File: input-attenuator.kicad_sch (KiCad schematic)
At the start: 92 parts, among them J1 DC_INTF, J2 RF_IN, J3 RX_1_RF, J4 RX_2_RF, K1 EE2-5TNU-L, K2 EE2-5TNU-L, K3 EE2-5TNU-L, K4 EE2-5TNU-L, Q1 BC858, Q2 BC858, Q3 MMBT3904, Q4 BC858, Q5 BC858, Q6 BC858, Q7 BC858, Q8 BC858, Q9 BC858, U1 74HC00, U2 74HC00, U3 74HC00, U4 74HC00, U5 74HC00, U6 74HC595

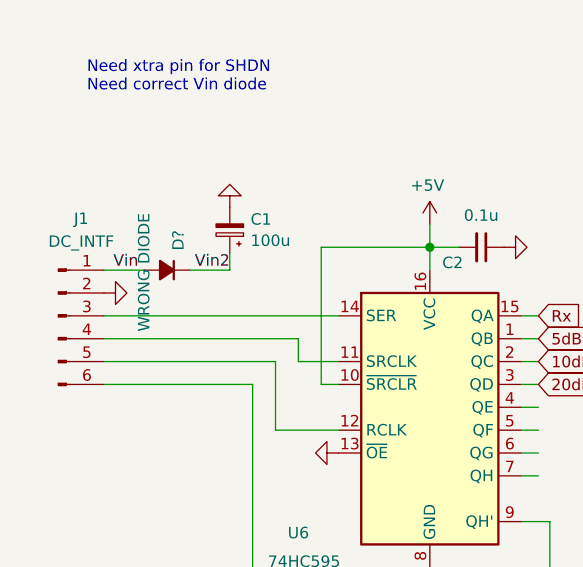
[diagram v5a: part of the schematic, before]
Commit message: Updated input pin header and Vin diode
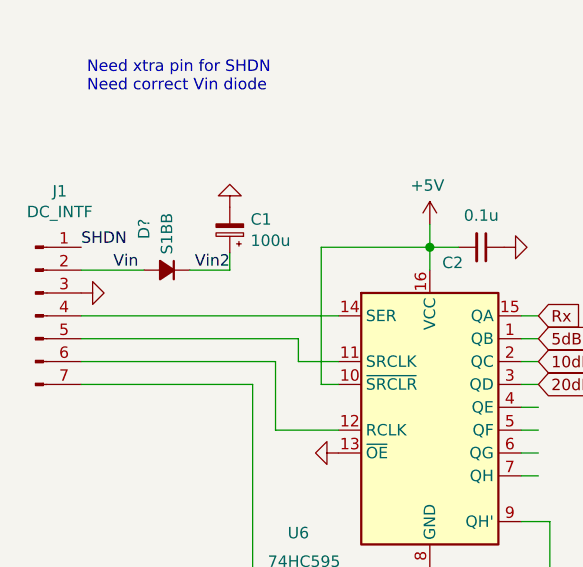
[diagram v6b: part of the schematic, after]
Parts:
- removed J1: DC_INTF, Connector_PinHeader_2.54mm:PinHeader_1x06_P2.54mm_Vertical, symbol Connector:Conn_01x06_Male
- added J1: DC_INTF, Connector_PinHeader_2.54mm:PinHeader_1x07_P2.54mm_Vertical, symbol Connector:Conn_01x07_Male
- D?: value WRONG DIODE -> S1BB; footprint Diode_SMD:D_SOD-323 -> Diode_SMD:D_SMB_Handsoldering
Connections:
- net GND: now also J1.3 (Pin_3)
- net SHDN: now also J1.1 (Pin_1)
- net Vin: now also J1.2 (Pin_2)
- net at U6.11 (SRCLK): now also J1.5 (Pin_5)
- net at U6.12 (RCLK): now also J1.6 (Pin_6)
- net at U6.14 (SER): now also J1.4 (Pin_4)
- net at U6.9 (QH'): now also J1.7 (Pin_7)
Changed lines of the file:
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@@
   (junction (at 259.715 40.005) (diameter 1.016) (color 0 0 0 0))
   (junction (at 259.715 57.15) (diameter 1.016) (color 0 0 0 0))
-  (wire (pts (xy 22.86 152.4) (xy 27.305 152.4))
+  (wire (pts (xy 20.32 152.4) (xy 27.305 152.4))
     (stroke (width 0) (type solid) (color 0 0 0 0))
   )
-  (wire (pts (xy 22.86 157.48) (xy 48.895 157.48))
+  (wire (pts (xy 20.32 157.48) (xy 48.895 157.48))
     (stroke (width 0) (type solid) (color 0 0 0 0))
   )
-  (wire (pts (xy 22.86 160.02) (xy 44.45 160.02))
+  (wire (pts (xy 20.32 160.02) (xy 44.45 160.02))
     (stroke (width 0) (type solid) (color 0 0 0 0))
   )
-  (wire (pts (xy 22.86 162.56) (xy 41.91 162.56))
+  (wire (pts (xy 20.32 162.56) (xy 41.91 162.56))
     (stroke (width 0) (type solid) (color 0 0 0 0))
   )
-  (wire (pts (xy 22.86 165.1) (xy 39.37 165.1))
+  (wire (pts (xy 20.32 165.1) (xy 39.37 165.1))
     (stroke (width 0) (type solid) (color 0 0 0 0))
   )
@@
     (effects (font (size 1.27 1.27)) (justify left bottom))
   )
+  (label "SHDN" (at 20.32 149.86 0)
+    (effects (font (size 1.27 1.27)) (justify left bottom))
+  )
   (label "PowerDn" (at 26.67 87.63 180)
     (effects (font (size 1.27 1.27)) (justify right bottom))
@@
     (pin "1")
   )
-  (symbol (lib_id "power:GND") (at 22.86 154.94 90) (unit 1)
+  (symbol (lib_id "power:GND") (at 20.32 154.94 90) (unit 1)
     (in_bom yes) (on_board yes)
-    (property "Reference" "#PWR0115" (id 0) (at 29.21 154.94 0)
+    (property "Reference" "#PWR0115" (id 0) (at 26.67 154.94 0)
       (effects (font (size 1.27 1.27)) hide)
     )
-    (property "Value" "GND" (id 1) (at 27.3558 154.813 0)
+    (property "Value" "GND" (id 1) (at 24.8158 154.813 0)
       (effects (font (size 1.27 1.27)) hide)
     )
-    (property "Footprint" "" (id 2) (at 22.86 154.94 0)
+    (property "Footprint" "" (id 2) (at 20.32 154.94 0)
       (effects (font (size 1.27 1.27)) hide)
     )
-    (property "Datasheet" "" (id 3) (at 22.86 154.94 0)
+    (property "Datasheet" "" (id 3) (at 20.32 154.94 0)
       (effects (font (size 1.27 1.27)) hide)
     )
@@
     (pin "2")
   )
+  (symbol (lib_id "Comparator:LM339") (at 149.225 172.085 0) (unit 5)
+    (in_bom yes) (on_board yes)
+    (property "Reference" "U?" (id 0) (at 149.225 162.7948 0))
+    (property "Value" "LP339" (id 1) (at 149.225 165.093 0))
+    (property "Footprint" "" (id 2) (at 147.955 169.545 0)
+      (effects (font (size 1.27 1.27)) hide)
+    )
+    (property "Datasheet" "https://www.st.com/resource/en/datasheet/lm139.pdf" (id 3) (at 150.495 167.005 0)
+      (effects (font (size 1.27 1.27)) hide)
+    )
+    (pin "12")
+    (pin "3")
+  )
   (symbol (lib_id "Device:D_Small_ALT") (at 29.21 49.53 270) (mirror x) (unit 1)
     (in_bom yes) (on_board yes)
@@
   (symbol (lib_id "Device:D_Small_ALT") (at 29.845 152.4 180) (unit 1)
     (in_bom yes) (on_board yes)
-    (property "Reference" "D?" (id 0) (at 31.115 147.955 90)
+    (property "Reference" "D?" (id 0) (at 27.305 146.685 90)
       (effects (font (size 1.27 1.27)) (justify left))
     )
-    (property "Value" "WRONG DIODE" (id 1) (at 27.305 146.05 90)
+    (property "Value" "S1BB" (id 1) (at 29.845 146.05 90)
       (effects (font (size 1.27 1.27)) (justify left))
     )
-    (property "Footprint" "Diode_SMD:D_SOD-323" (id 2) (at 29.845 152.4 90)
+    (property "Footprint" "Diode_SMD:D_SMB_Handsoldering" (id 2) (at 29.845 152.4 90)
       (effects (font (size 1.27 1.27)) hide)
     )
@@
     (pin "7")
   )
-  (symbol (lib_id "Comparator:LM339") (at 149.225 172.085 0) (unit 5)
-    (in_bom yes) (on_board yes)
-    (property "Reference" "U?" (id 0) (at 149.225 162.7948 0))
-    (property "Value" "LP339" (id 1) (at 149.225 165.093 0))
-    (property "Footprint" "" (id 2) (at 147.955 169.545 0)
-      (effects (font (size 1.27 1.27)) hide)
-    )
-    (property "Datasheet" "https://www.st.com/resource/en/datasheet/lm139.pdf" (id 3) (at 150.495 167.005 0)
-      (effects (font (size 1.27 1.27)) hide)
-    )
-    (pin "12")
-    (pin "3")
-  )
   (symbol (lib_id "Connector:Conn_Coaxial") (at 19.685 32.385 0) (mirror y) (unit 1)
     (in_bom yes) (on_board yes)
@@
     (pin "2")
   )
-  (symbol (lib_id "Connector:Conn_01x06_Male") (at 17.78 157.48 0) (unit 1)
+  (symbol (lib_id "Connector:Conn_01x07_Male") (at 15.24 157.48 0) (unit 1)
     (in_bom yes) (on_board yes)
-    (property "Reference" "J1" (id 0) (at 20.32 146.685 0))
-    (property "Value" "DC_INTF" (id 1) (at 20.32 149.225 0))
-    (property "Footprint" "Connector_PinHeader_2.54mm:PinHeader_1x06_P2.54mm_Vertical" (id 2) (at 17.78 157.48 0)
+    (property "Reference" "J1" (id 0) (at 17.9324 143.6328 0))
+    (property "Value" "DC_INTF" (id 1) (at 17.9324 145.9315 0))
+    (property "Footprint" "Connector_PinHeader_2.54mm:PinHeader_1x07_P2.54mm_Vertical" (id 2) (at 15.24 157.48 0)
       (effects (font (size 1.27 1.27)) hide)
     )
-    (property "Datasheet" "~" (id 3) (at 17.78 157.48 0)
+    (property "Datasheet" "~" (id 3) (at 15.24 157.48 0)
       (effects (font (size 1.27 1.27)) hide)
     )
@@
     (pin "5")
     (pin "6")
+    (pin "7")
   )
   (symbol (lib_id "Transistor_BJT:BC858") (at 40.64 66.04 0) (mirror y) (unit 1)
@@
     )
     (path "/9801f823-24c1-4f5d-bf6c-e2a3a0a8f252"
-      (reference "D?") (unit 1) (value "WRONG DIODE") (footprint "Diode_SMD:D_SOD-323")
+      (reference "D?") (unit 1) (value "S1BB") (footprint "Diode_SMD:D_SMB_Handsoldering")
     )
-    (path "/00000000-0000-0000-0000-00005f2d8ca1"
-      (reference "J1") (unit 1) (value "DC_INTF") (footprint "Connector_PinHeader_2.54mm:PinHeader_1x06_P2.54mm_Vertical")
+    (path "/92e7aac3-ac59-4653-8577-27b028dac29e"
+      (reference "J1") (unit 1) (value "DC_INTF") (footprint "Connector_PinHeader_2.54mm:PinHeader_1x07_P2.54mm_Vertical")
     )
     (path "/5687a9c9-05f1-4ecb-9b08-f88b6a240510"

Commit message: lookAtC
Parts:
- removed K? (x3): EE2-5TNU-L, Relay_SMD:Relay_DPDT_Kemet_EE2_NU_DoubleCoil, symbol rf-designers:EE2-5TNU-L
- removed R?: 180k, Resistor_SMD:R_0805_2012Metric, symbol Device:R_Small_US
- removed R? (x2): 1M, Resistor_SMD:R_0805_2012Metric, symbol Device:R_Small_US
- added J2: DC_INTF, Connector_PinHeader_2.54mm:PinHeader_1x07_P2.54mm_Vertical, symbol Connector:Conn_01x07_Male
- C1: value 100u -> 10000u
- U8: renamed from U?; footprint (none) -> Package_SO:SO-14_3.9x8.65mm_P1.27mm
- gave numbers to parts that had none: 16
- renumbered J2 to J5
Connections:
- net +5V: now also U8.6 (-); no longer U8.4 (-)
- net GND: now also J1.2 (Pin_2), J2.2 (Pin_2); no longer J1.3 (Pin_3)
- net PowerDn: now also U8.1; no longer U8.2
- net SHDN: now also J1.7 (Pin_7), J2.7 (Pin_7); no longer J1.1 (Pin_1)
- net Vin: now also J1.1 (Pin_1), J2.1 (Pin_1); no longer J1.2 (Pin_2)
- net at U6.11 (SRCLK): now also J1.4 (Pin_4), J2.4 (Pin_4); no longer J1.5 (Pin_5)
- net at U6.12 (RCLK): now also J1.5 (Pin_5); no longer J1.6 (Pin_6)
- net at U6.14 (SER): now also J1.3 (Pin_3), J2.3 (Pin_3); no longer J1.4 (Pin_4)
- net at U6.9 (QH'): now also J1.6 (Pin_6), J2.5 (Pin_5); no longer J1.7 (Pin_7)
- net at R31.1, R33.1, U8.2: now also U8.7 (+); no longer U8.5 (+)
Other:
- note added: "To next shift register"
- note removed: "Need xtra pin for SHDN Need correct Vin diode"
- moved on the sheet: J1

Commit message: final
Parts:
- removed unit 2 of U8
- added C8: 2200u, Capacitor_THT:CP_Radial_D12.5mm_P7.50mm, symbol Device:CP_Small
- C1: value 10000u -> 2200u; footprint Capacitor_SMD:CP_Elec_6.3x5.4_Nichicon -> Capacitor_THT:CP_Radial_D12.5mm_P7.50mm
- U6: footprint Package_SO:SO-16_5.3x10.2mm_P1.27mm -> Package_SO:SO-16_3.9x9.9mm_P1.27mm
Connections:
- net 20dB: now also U6.1 (QB); no longer U6.3 (QD)
- net 5dB: now also U6.3 (QD); no longer U6.1 (QB)
- net GND: now also C8.2
- net PowerDn: now also R31.1, R33.1, U8.2
- net Vin2: now also C8.1
- net at J1.4 (Pin_4), J2.4 (Pin_4): now also U6.12 (RCLK); no longer U6.11 (SRCLK)
- net at J1.5 (Pin_5): now also U6.11 (SRCLK); no longer U6.12 (RCLK)
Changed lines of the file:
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@@
   (junction (at 29.845 160.02) (diameter 1.016) (color 0 0 0 0))
   (junction (at 32.385 165.1) (diameter 1.016) (color 0 0 0 0))
+  (junction (at 36.83 152.4) (diameter 1.016) (color 0 0 0 0))
   (junction (at 38.1 40.005) (diameter 1.016) (color 0 0 0 0))
   (junction (at 38.1 57.15) (diameter 1.016) (color 0 0 0 0))
@@
     (stroke (width 0) (type solid) (color 0 0 0 0))
   )
-  (wire (pts (xy 20.32 162.56) (xy 41.91 162.56))
+  (wire (pts (xy 20.32 162.56) (xy 48.895 162.56))
     (stroke (width 0) (type solid) (color 0 0 0 0))
   )
@@
     (stroke (width 0) (type solid) (color 0 0 0 0))
   )
+  (wire (pts (xy 36.83 152.4) (xy 40.64 152.4))
+    (stroke (width 0) (type solid) (color 0 0 0 0))
+  )
   (wire (pts (xy 38.1 38.1) (xy 38.1 40.005))
     (stroke (width 0) (type solid) (color 0 0 0 0))
@@
     (stroke (width 0) (type solid) (color 0 0 0 0))
   )
-  (wire (pts (xy 41.91 85.09) (xy 46.99 85.09))
-    (stroke (width 0) (type solid) (color 0 0 0 0))
-  )
-  (wire (pts (xy 41.91 90.805) (xy 41.91 85.09))
+  (wire (pts (xy 40.64 152.4) (xy 40.64 150.495))
     (stroke (width 0) (type solid) (color 0 0 0 0))
   )
-  (wire (pts (xy 41.91 162.56) (xy 41.91 170.18))
+  (wire (pts (xy 41.91 85.09) (xy 46.99 85.09))
     (stroke (width 0) (type solid) (color 0 0 0 0))
   )
-  (wire (pts (xy 41.91 170.18) (xy 48.895 170.18))
+  (wire (pts (xy 41.91 90.805) (xy 41.91 85.09))
     (stroke (width 0) (type solid) (color 0 0 0 0))
   )
-  (wire (pts (xy 44.45 160.02) (xy 44.45 162.56))
+  (wire (pts (xy 44.45 160.02) (xy 44.45 170.18))
     (stroke (width 0) (type solid) (color 0 0 0 0))
   )
-  (wire (pts (xy 44.45 162.56) (xy 48.895 162.56))
+  (wire (pts (xy 44.45 170.18) (xy 48.895 170.18))
     (stroke (width 0) (type solid) (color 0 0 0 0))
   )
@@
     (stroke (width 0) (type solid) (color 0 0 0 0))
   )
+  (wire (pts (xy 163.195 127) (xy 163.195 124.46))
+    (stroke (width 0) (type solid) (color 0 0 0 0))
+  )
+  (wire (pts (xy 163.195 127) (xy 180.34 127))
+    (stroke (width 0) (type solid) (color 0 0 0 0))
+  )
   (wire (pts (xy 165.1 38.1) (xy 165.1 40.005))
     (stroke (width 0) (type solid) (color 0 0 0 0))
@@
     (stroke (width 0) (type solid) (color 0 0 0 0))
   )
-  (wire (pts (xy 178.435 127) (xy 180.34 127))
-    (stroke (width 0) (type solid) (color 0 0 0 0))
-  )
   (wire (pts (xy 180.34 127) (xy 180.34 137.795))
     (stroke (width 0) (type solid) (color 0 0 0 0))
@@
     )
   )
-  (global_label "5dB" (shape input) (at 71.12 160.02 0)
+  (global_label "20dB" (shape input) (at 71.12 160.02 0)
     (effects (font (size 1.27 1.27)) (justify left))
-    (property "Intersheet References" "${INTERSHEET_REFS}" (id 0) (at 78.6857 159.9406 0)
+    (property "Intersheet References" "${INTERSHEET_REFS}" (id 0) (at 79.8952 159.9406 0)
       (effects (font (size 1.27 1.27)) (justify left) hide)
     )
@@
     )
   )
-  (global_label "20dB" (shape input) (at 71.12 165.1 0)
+  (global_label "5dB" (shape input) (at 71.12 165.1 0)
     (effects (font (size 1.27 1.27)) (justify left))
-    (property "Intersheet References" "${INTERSHEET_REFS}" (id 0) (at 79.8952 165.0206 0)
+    (property "Intersheet References" "${INTERSHEET_REFS}" (id 0) (at 78.6857 165.0206 0)
       (effects (font (size 1.27 1.27)) (justify left) hide)
     )
@@
     (pin "1")
   )
-  (symbol (lib_id "power:+5V") (at 163.195 129.54 90) (unit 1)
-    (in_bom yes) (on_board yes)
-    (property "Reference" "#PWR0148" (id 0) (at 167.005 129.54 0)
-      (effects (font (size 1.27 1.27)) hide)
-    )
-    (property "Value" "+5V" (id 1) (at 158.8706 129.1717 0))
-    (property "Footprint" "" (id 2) (at 163.195 129.54 0)
-      (effects (font (size 1.27 1.27)) hide)
-    )
-    (property "Datasheet" "" (id 3) (at 163.195 129.54 0)
-      (effects (font (size 1.27 1.27)) hide)
-    )
-    (pin "1")
-  )
   (symbol (lib_id "power:+5V") (at 165.1 71.12 180) (unit 1)
     (in_bom yes) (on_board yes)
@@
     (pin "1")
   )
+  (symbol (lib_id "power:GND") (at 40.64 145.415 180) (unit 1)
+    (in_bom yes) (on_board yes)
+    (property "Reference" "#PWR0153" (id 0) (at 40.64 139.065 0)
+      (effects (font (size 1.27 1.27)) hide)
+    )
+    (property "Value" "GND" (id 1) (at 40.513 140.9192 0)
+      (effects (font (size 1.27 1.27)) hide)
+    )
+    (property "Footprint" "" (id 2) (at 40.64 145.415 0)
+      (effects (font (size 1.27 1.27)) hide)
+    )
+    (property "Datasheet" "" (id 3) (at 40.64 145.415 0)
+      (effects (font (size 1.27 1.27)) hide)
+    )
+    (pin "1")
+  )
   (symbol (lib_id "power:GND") (at 41.91 95.885 270) (unit 1)
     (in_bom yes) (on_board yes)
@@
       (effects (font (size 1.27 1.27)) (justify right))
     )
-    (property "Value" "10000u" (id 1) (at 39.1414 149.1234 0)
+    (property "Value" "2200u" (id 1) (at 39.141 149.123 0)
       (effects (font (size 1.27 1.27)) (justify right))
     )
-    (property "Footprint" "Capacitor_SMD:CP_Elec_6.3x5.4_Nichicon" (id 2) (at 36.83 147.955 0)
+    (property "Footprint" "Capacitor_THT:CP_Radial_D12.5mm_P7.50mm" (id 2) (at 36.83 147.955 0)
       (effects (font (size 1.27 1.27)) hide)
     )
@@
     (pin "2")
   )
+  (symbol (lib_id "Device:CP_Small") (at 40.64 147.955 180) (unit 1)
+    (in_bom yes) (on_board yes)
+    (property "Reference" "C8" (id 0) (at 42.9514 146.7612 0)
+      (effects (font (size 1.27 1.27)) (justify right))
+    )
+    (property "Value" "2200u" (id 1) (at 42.951 149.123 0)
+      (effects (font (size 1.27 1.27)) (justify right))
+    )
+    (property "Footprint" "Capacitor_THT:CP_Radial_D12.5mm_P7.50mm" (id 2) (at 40.64 147.955 0)
+      (effects (font (size 1.27 1.27)) hide)
+    )
+    (property "Datasheet" "~" (id 3) (at 40.64 147.955 0)
+      (effects (font (size 1.27 1.27)) hide)
+    )
+    (pin "1")
+    (pin "2")
+  )
   (symbol (lib_id "Device:C_Small") (at 44.45 95.885 270) (unit 1)
     (in_bom yes) (on_board yes)
@@
     (pin "5")
   )
-  (symbol (lib_id "Comparator:LM339") (at 170.815 127 0) (unit 2)
-    (in_bom yes) (on_board yes)
-    (property "Reference" "U8" (id 0) (at 168.91 127.235 0))
-    (property "Value" "LP339" (id 1) (at 172.085 132.074 0))
-    (property "Footprint" "Package_SO:SO-14_3.9x8.65mm_P1.27mm" (id 2) (at 169.545 124.46 0)
-      (effects (font (size 1.27 1.27)) hide)
-    )
-    (property "Datasheet" "https://www.st.com/resource/en/datasheet/lm139.pdf" (id 3) (at 172.085 121.92 0)
-      (effects (font (size 1.27 1.27)) hide)
-    )
-    (pin "1")
-    (pin "6")
-    (pin "7")
-  )
   (symbol (lib_id "74xx:74HC00") (at 90.805 172.72 0) (unit 5)
     (in_bom yes) (on_board yes)
@@
     (property "Reference" "U6" (id 0) (at 44.45 181.61 0))
     (property "Value" "74HC595" (id 1) (at 45.085 184.785 0))
-    (property "Footprint" "Package_SO:SO-16_5.3x10.2mm_P1.27mm" (id 2) (at 59.055 167.64 0)
+    (property "Footprint" "Package_SO:SO-16_3.9x9.9mm_P1.27mm" (id 2) (at 59.055 167.64 0)
       (effects (font (size 1.27 1.27)) hide)
     )
@@
       (reference "#PWR0147") (unit 1) (value "GND") (footprint "")
     )
-    (path "/580483ba-39e3-4efc-8eeb-6522e33be8e8"
-      (reference "#PWR0148") (unit 1) (value "+5V") (footprint "")
-    )
     (path "/c947ab05-4742-494e-b7fe-632a05628c8f"
       (reference "#PWR0149") (unit 1) (value "GND") (footprint "")
@@
       (reference "#PWR0152") (unit 1) (value "GND") (footprint "")
     )
+    (path "/3e44b944-75b2-458b-a4b6-319ed679d7aa"
+      (reference "#PWR0153") (unit 1) (value "GND") (footprint "")
+    )
     (path "/00000000-0000-0000-0000-00005f2f2f18"
-      (reference "C1") (unit 1) (value "10000u") (footprint "Capacitor_SMD:CP_Elec_6.3x5.4_Nichicon")
+      (reference "C1") (unit 1) (value "2200u") (footprint "Capacitor_THT:CP_Radial_D12.5mm_P7.50mm")
     )
     (path "/00000000-0000-0000-0000-00005f2ebfc9"
@@
       (reference "C7") (unit 1) (value "0.22u") (footprint "Capacitor_SMD:C_0805_2012Metric")
     )
+    (path "/7699ad8e-2776-4a76-aa81-f71fb3040c25"
+      (reference "C8") (unit 1) (value "2200u") (footprint "Capacitor_THT:CP_Radial_D12.5mm_P7.50mm")
+    )
     (path "/00000000-0000-0000-0000-00005f1e54e1"
       (reference "D1") (unit 1) (value "1N4148WS") (footprint "Diode_SMD:D_SOD-323")
@@
     )
     (path "/00000000-0000-0000-0000-00005f259000"
-      (reference "U6") (unit 1) (value "74HC595") (footprint "Package_SO:SO-16_5.3x10.2mm_P1.27mm")
+      (reference "U6") (unit 1) (value "74HC595") (footprint "Package_SO:SO-16_3.9x9.9mm_P1.27mm")
     )
     (path "/8354ecd4-2a4f-44f8-a737-ff9cdb5f7927"
@@
       (reference "U8") (unit 1) (value "LP339") (footprint "Package_SO:SO-14_3.9x8.65mm_P1.27mm")
     )
-    (path "/83430977-3e55-4b8c-bc38-a585c8d1731b"
-      (reference "U8") (unit 2) (value "LP339") (footprint "Package_SO:SO-14_3.9x8.65mm_P1.27mm")
-    )
     (path "/b903cbde-9215-48dd-89f9-54d7dabe3bb1"
